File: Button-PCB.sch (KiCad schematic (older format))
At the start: 32 parts

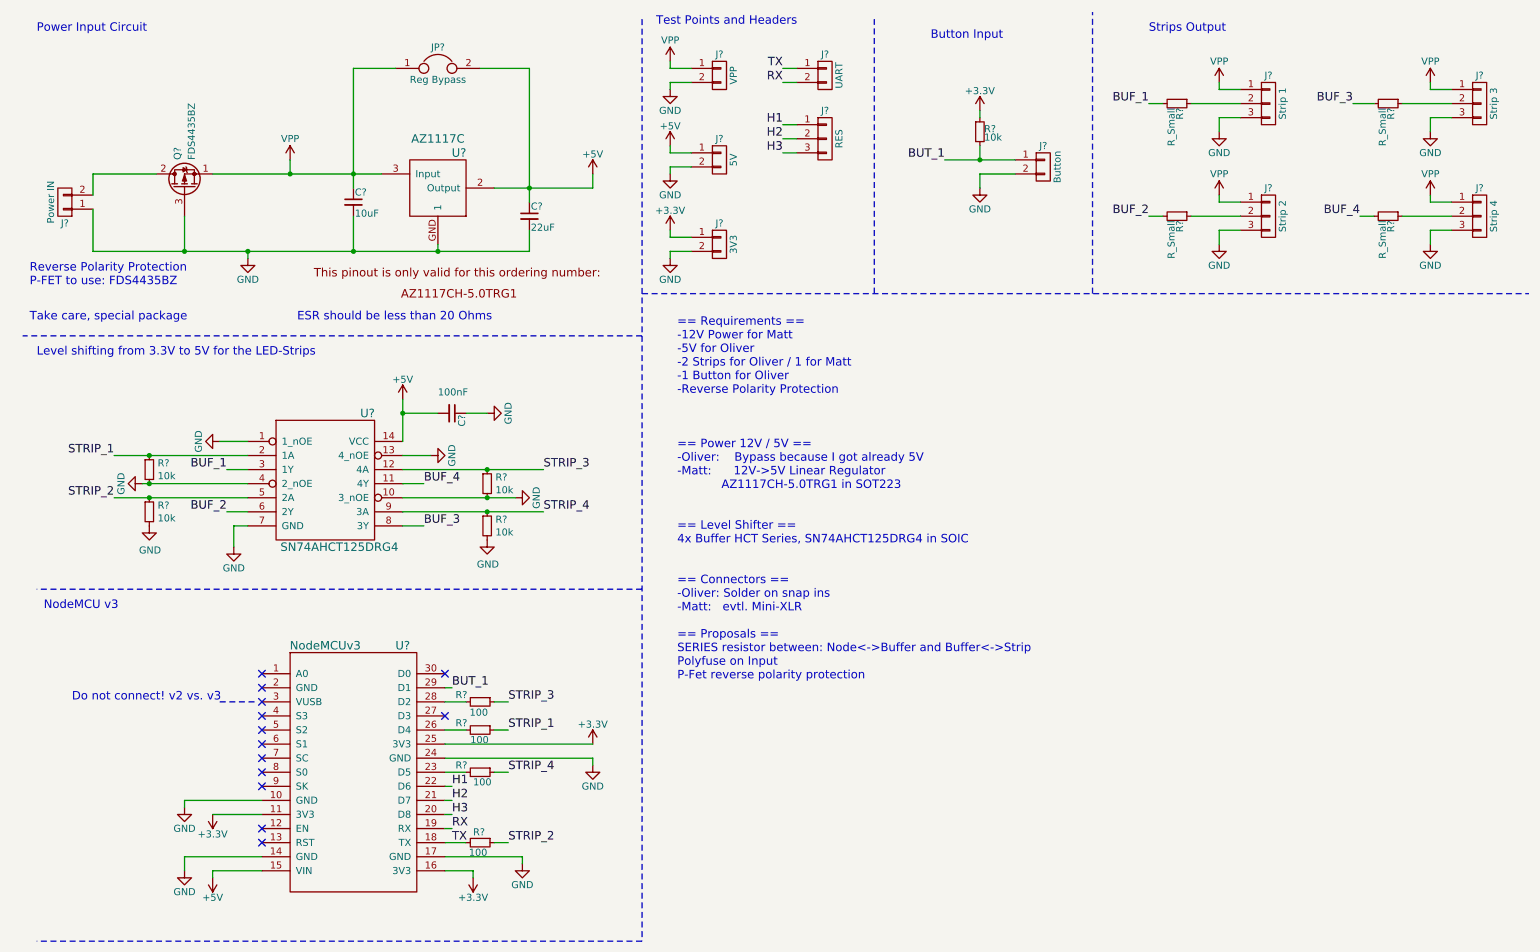
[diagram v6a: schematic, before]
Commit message: Moving series termination of strips to source and assigning 100R
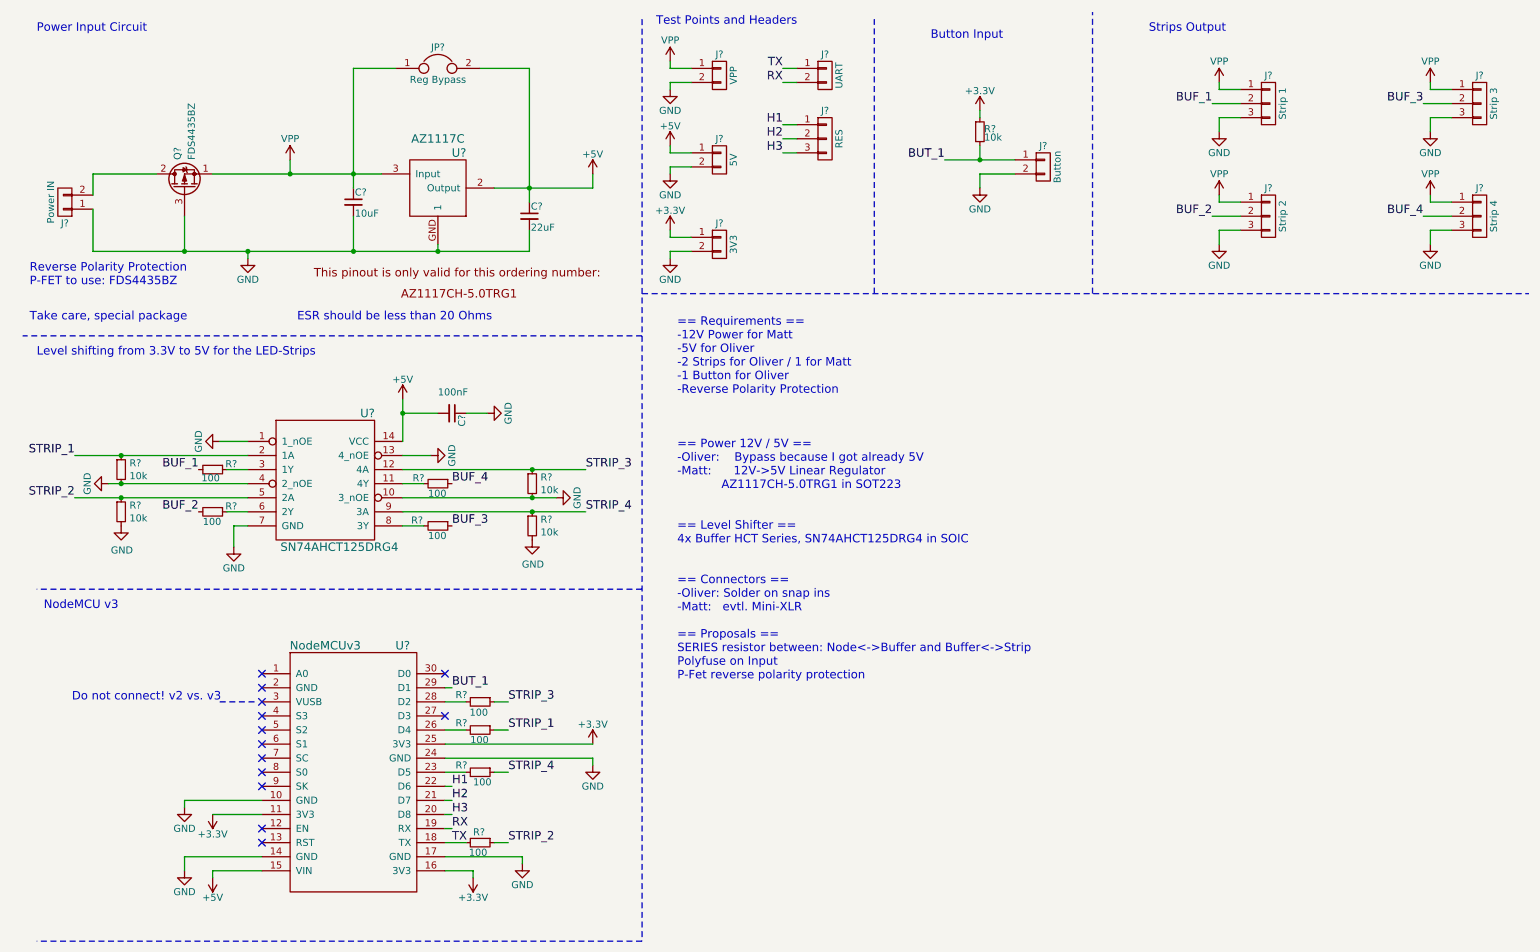
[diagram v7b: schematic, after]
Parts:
- R? (x4): value R_Small -> 100
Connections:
- net BUF_1: now also J?.2 (P2); no longer U?.3 (1Y)
- net BUF_2: now also J?.2 (P2); no longer U?.6 (2Y)
- net BUF_3: now also J?.2 (P2), R?.1; no longer R?.2, U?.8 (3Y)
- net BUF_4: now also J?.2 (P2), R?.1; no longer R?.2, U?.11 (4Y)
- net at R?.1: now also U?.6 (2Y); no longer J?.2 (P2)
- net at R?.1: now also U?.3 (1Y); no longer J?.2 (P2)
- new net: R?.2, U?.8 (3Y)
- new net: R?.2, U?.11 (4Y)
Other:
- moved on the sheet: R?
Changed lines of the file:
@@
 L R_Small R?
 U 1 1 593DD67C
-P 8700 1150
-F 0 "R?" H 8730 1170 50  0000 L CNN
-F 1 "R_Small" H 8730 1110 50  0000 L CNN
-F 2 "" H 8700 1150 50  0001 C CNN
-F 3 "" H 8700 1150 50  0001 C CNN
-	1    8700 1150
+P 1850 3750
+F 0 "R?" V 1810 3840 50  0000 L CNN
+F 1 "100" V 1910 3670 50  0000 L CNN
+F 2 "" H 1850 3750 50  0001 C CNN
+F 3 "" H 1850 3750 50  0001 C CNN
+	1    1850 3750
 	0    1    1    0
 $EndComp
@@
 L R_Small R?
 U 1 1 593DD71A
-P 8700 1950
-F 0 "R?" H 8730 1970 50  0000 L CNN
-F 1 "R_Small" H 8730 1910 50  0000 L CNN
-F 2 "" H 8700 1950 50  0001 C CNN
-F 3 "" H 8700 1950 50  0001 C CNN
-	1    8700 1950
+P 1850 4050
+F 0 "R?" V 1810 4140 50  0000 L CNN
+F 1 "100" V 1920 3980 50  0000 L CNN
+F 2 "" H 1850 4050 50  0001 C CNN
+F 3 "" H 1850 4050 50  0001 C CNN
+	1    1850 4050
 	0    1    1    0
 $EndComp
@@
 	9000 2050 9150 2050
 Wire Wire Line
-	9150 1950 8800 1950
+	9150 1950 8950 1950
 Wire Wire Line
 	9150 1250 9000 1250
@@
 	9000 1250 9000 1350
 Wire Wire Line
-	9150 1150 8800 1150
+	9150 1150 8950 1150
 Wire Wire Line
 	7300 1750 7300 1650
@@
 L R_Small R?
 U 1 1 593F28B5
-P 10200 1150
-F 0 "R?" H 10230 1170 50  0000 L CNN
-F 1 "R_Small" H 10230 1110 50  0000 L CNN
-F 2 "" H 10200 1150 50  0001 C CNN
-F 3 "" H 10200 1150 50  0001 C CNN
-	1    10200 1150
+P 3450 4150
+F 0 "R?" V 3410 3960 50  0000 L CNN
+F 1 "100" V 3520 4080 50  0000 L CNN
+F 2 "" H 3450 4150 50  0001 C CNN
+F 3 "" H 3450 4150 50  0001 C CNN
+	1    3450 4150
 	0    1    1    0
 $EndComp
@@
 L R_Small R?
 U 1 1 593F28BB
-P 10200 1950
-F 0 "R?" H 10230 1970 50  0000 L CNN
-F 1 "R_Small" H 10230 1910 50  0000 L CNN
-F 2 "" H 10200 1950 50  0001 C CNN
-F 3 "" H 10200 1950 50  0001 C CNN
-	1    10200 1950
+P 3450 3850
+F 0 "R?" V 3410 3670 50  0000 L CNN
+F 1 "100" V 3520 3780 50  0000 L CNN
+F 2 "" H 3450 3850 50  0001 C CNN
+F 3 "" H 3450 3850 50  0001 C CNN
+	1    3450 3850
 	0    1    1    0
 $EndComp
@@
 	10500 2050 10650 2050
 Wire Wire Line
-	10650 1950 10300 1950
+	10650 1950 10450 1950
 Wire Wire Line
 	10650 1250 10500 1250
@@
 	10500 1250 10500 1350
 Wire Wire Line
-	10650 1150 10300 1150
+	10650 1150 10450 1150
 Wire Wire Line
 	9000 1000 9000 1050
@@
 Wire Wire Line
 	10500 1050 10650 1050
-Text Label 8500 1950 2    60   ~ 0
+Text Label 8950 1950 2    60   ~ 0
 BUF_2
-Text Label 8500 1150 2    60   ~ 0
+Text Label 8950 1150 2    60   ~ 0
 BUF_1
-Text Label 9950 1150 2    60   ~ 0
+Text Label 10450 1150 2    60   ~ 0
 BUF_3
-Text Label 10000 1950 2    60   ~ 0
+Text Label 10450 1950 2    60   ~ 0
 BUF_4
-Wire Wire Line
-	8500 1150 8600 1150
-Wire Wire Line
-	8500 1950 8600 1950
-Wire Wire Line
-	10000 1950 10100 1950
-Wire Wire Line
-	9950 1150 10100 1150
 Wire Notes Line
 	4900 2500 11200 2500
@@
 L GND #PWR?
 U 1 1 5942C499
-P 4000 3950
-F 0 "#PWR?" H 4000 3700 50  0001 C CNN
-F 1 "GND" H 4000 3800 50  0000 C CNN
-F 2 "" H 4000 3950 50  0001 C CNN
-F 3 "" H 4000 3950 50  0001 C CNN
-	1    4000 3950
+P 4290 3950
+F 0 "#PWR?" H 4290 3700 50  0001 C CNN
+F 1 "GND" H 4290 3800 50  0000 C CNN
+F 2 "" H 4290 3950 50  0001 C CNN
+F 3 "" H 4290 3950 50  0001 C CNN
+	1    4290 3950
 	0    -1   -1   0
 $EndComp
-Text Label 1150 3950 2    60   ~ 0
+Text Label 870  3950 2    60   ~ 0
 STRIP_2
-Text Label 1150 3650 2    60   ~ 0
+Text Label 870  3650 2    60   ~ 0
 STRIP_1
-Text Label 4200 3750 0    60   ~ 0
+Text Label 4500 3750 0    60   ~ 0
 STRIP_3
-Text Label 4200 4050 0    60   ~ 0
+Text Label 4500 4050 0    60   ~ 0
 STRIP_4
 $Comp
@@
 	0    1    1    0
 $EndComp
-Text Label 1950 3750 2    60   ~ 0
+Text Label 1750 3750 2    60   ~ 0
 BUF_1
-Text Label 1950 4050 2    60   ~ 0
+Text Label 1750 4050 2    60   ~ 0
 BUF_2
-Text Label 3350 4150 0    60   ~ 0
+Text Label 3550 4150 0    60   ~ 0
 BUF_3
-Text Label 3350 3850 0    60   ~ 0
+Text Label 3550 3850 0    60   ~ 0
 BUF_4
 Wire Wire Line
@@
 	1950 3750 2100 3750
 Wire Wire Line
-	1150 3650 1400 3650
-Wire Wire Line
-	1400 3650 2100 3650
-Wire Wire Line
-	1150 3950 1400 3950
-Wire Wire Line
-	1400 3950 2100 3950
+	870  3650 1200 3650
+Wire Wire Line
+	1200 3650 2100 3650
+Wire Wire Line
+	870  3950 1200 3950
+Wire Wire Line
+	1200 3950 2100 3950
 $Comp
 L GND #PWR?
 U 1 1 5942E71C
-P 1350 3850
-F 0 "#PWR?" H 1350 3600 50  0001 C CNN
-F 1 "GND" H 1350 3700 50  0000 C CNN
-F 2 "" H 1350 3850 50  0001 C CNN
-F 3 "" H 1350 3850 50  0001 C CNN
-	1    1350 3850
+P 1110 3850
+F 0 "#PWR?" H 1110 3600 50  0001 C CNN
+F 1 "GND" H 1110 3700 50  0000 C CNN
+F 2 "" H 1110 3850 50  0001 C CNN
+F 3 "" H 1110 3850 50  0001 C CNN
+	1    1110 3850
 	0    1    1    0
 $EndComp
 Wire Wire Line
-	1350 3850 1400 3850
-Wire Wire Line
-	1400 3850 2100 3850
+	1110 3850 1200 3850
+Wire Wire Line
+	1200 3850 2100 3850
 $Comp
 L GND #PWR?
@@
 	1900 3550 2100 3550
 Wire Wire Line
-	3200 3950 3800 3950
-Wire Wire Line
-	3800 3950 4000 3950
+	3200 3950 4120 3950
+Wire Wire Line
+	4120 3950 4290 3950
 Wire Wire Line
 	3400 3650 3200 3650
@@
 $EndComp
 Wire Wire Line
-	3200 3750 3800 3750
-Wire Wire Line
-	3800 3750 4200 3750
-Wire Wire Line
-	3200 4050 3800 4050
-Wire Wire Line
-	3800 4050 4200 4050
+	3200 3750 4120 3750
+Wire Wire Line
+	4120 3750 4500 3750
+Wire Wire Line
+	3200 4050 4120 4050
+Wire Wire Line
+	4120 4050 4500 4050
 $Comp
 L C_Small C?
@@
 L R_Small R?
 U 1 1 5945C430
-P 1400 4050
-F 0 "R?" H 1459 4096 50  0000 L CNN
-F 1 "10k" H 1459 4005 50  0000 L CNN
-F 2 "" H 1400 4050 50  0001 C CNN
-F 3 "" H 1400 4050 50  0001 C CNN
-	1    1400 4050
+P 1200 4050
+F 0 "R?" H 1259 4096 50  0000 L CNN
+F 1 "10k" H 1259 4005 50  0000 L CNN
+F 2 "" H 1200 4050 50  0001 C CNN
+F 3 "" H 1200 4050 50  0001 C CNN
+	1    1200 4050
 	1    0    0    -1
 $EndComp
@@
 L R_Small R?
 U 1 1 5945C4B9
-P 1400 3750
-F 0 "R?" H 1459 3796 50  0000 L CNN
-F 1 "10k" H 1459 3705 50  0000 L CNN
-F 2 "" H 1400 3750 50  0001 C CNN
-F 3 "" H 1400 3750 50  0001 C CNN
-	1    1400 3750
+P 1200 3750
+F 0 "R?" H 1259 3796 50  0000 L CNN
+F 1 "10k" H 1259 3705 50  0000 L CNN
+F 2 "" H 1200 3750 50  0001 C CNN
+F 3 "" H 1200 3750 50  0001 C CNN
+	1    1200 3750
 	1    0    0    -1
 $EndComp
@@
 L R_Small R?
 U 1 1 5945C541
-P 3800 3850
-F 0 "R?" H 3859 3896 50  0000 L CNN
-F 1 "10k" H 3859 3805 50  0000 L CNN
-F 2 "" H 3800 3850 50  0001 C CNN
-F 3 "" H 3800 3850 50  0001 C CNN
-	1    3800 3850
+P 4120 3850
+F 0 "R?" H 4179 3896 50  0000 L CNN
+F 1 "10k" H 4179 3805 50  0000 L CNN
+F 2 "" H 4120 3850 50  0001 C CNN
+F 3 "" H 4120 3850 50  0001 C CNN
+	1    4120 3850
 	1    0    0    -1
 $EndComp
@@
 L R_Small R?
 U 1 1 5945C5D0
-P 3800 4150
-F 0 "R?" H 3859 4196 50  0000 L CNN
-F 1 "10k" H 3859 4105 50  0000 L CNN
-F 2 "" H 3800 4150 50  0001 C CNN
-F 3 "" H 3800 4150 50  0001 C CNN
-	1    3800 4150
-	1    0    0    -1
-$EndComp
-Connection ~ 3800 3750
-Connection ~ 3800 4050
-Connection ~ 1400 3650
-Connection ~ 1400 3950
-Connection ~ 1400 3850
+P 4120 4150
+F 0 "R?" H 4179 4196 50  0000 L CNN
+F 1 "10k" H 4179 4105 50  0000 L CNN
+F 2 "" H 4120 4150 50  0001 C CNN
+F 3 "" H 4120 4150 50  0001 C CNN
+	1    4120 4150
+	1    0    0    -1
+$EndComp
+Connection ~ 4120 3750
+Connection ~ 4120 4050
+Connection ~ 1200 3650
+Connection ~ 1200 3950
+Connection ~ 1200 3850
 $Comp
 L GND #PWR?
 U 1 1 5945C779
-P 1400 4150
-F 0 "#PWR?" H 1400 3900 50  0001 C CNN
-F 1 "GND" H 1405 3977 50  0000 C CNN
-F 2 "" H 1400 4150 50  0001 C CNN
-F 3 "" H 1400 4150 50  0001 C CNN
-	1    1400 4150
+P 1200 4150
+F 0 "#PWR?" H 1200 3900 50  0001 C CNN
+F 1 "GND" H 1205 3977 50  0000 C CNN
+F 2 "" H 1200 4150 50  0001 C CNN
+F 3 "" H 1200 4150 50  0001 C CNN
+	1    1200 4150
 	1    0    0    -1
 $EndComp
@@
 L GND #PWR?
 U 1 1 5945C810
-P 3800 4250
-F 0 "#PWR?" H 3800 4000 50  0001 C CNN
-F 1 "GND" H 3805 4077 50  0000 C CNN
-F 2 "" H 3800 4250 50  0001 C CNN
-F 3 "" H 3800 4250 50  0001 C CNN
-	1    3800 4250
-	1    0    0    -1
-$EndComp
-Connection ~ 3800 3950
+P 4120 4250
+F 0 "#PWR?" H 4120 4000 50  0001 C CNN
+F 1 "GND" H 4125 4077 50  0000 C CNN
+F 2 "" H 4120 4250 50  0001 C CNN
+F 3 "" H 4120 4250 50  0001 C CNN
+	1    4120 4250
+	1    0    0    -1
+$EndComp
+Connection ~ 4120 3950
 Wire Wire Line
 	3950 5600 3850 5600
